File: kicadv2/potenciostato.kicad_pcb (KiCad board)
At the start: 2 copper layers, 100 x 100 mm, 56 parts, among them J1 USB_B_Micro, J10 test_GND, J11 test_GND, J12 test_GND, J13 AC2, J2 test_DAC, J3 Conn_01x03_Male, J4 test_I, J5 test_V, J6 test_VIN, J7 test_I, J8 test_V, J9 AC1, U1 OP77, U2 TL082, U3 OP77, U4 OP77, U5 4316, U6 L7805, U7 TL064, U8 L7905, U9 TL082

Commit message: movido USB
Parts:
- moved J1 23.7 mm to (199.7, 144.1)
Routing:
- net Net-(J1-Pad3): track 107.4 -> 41.7 mm, vias 1 -> 0
- net Net-(J1-Pad2): track 109.4 -> 45.7 mm, vias 1 -> 0
- net GND: track 0.00 -> 19.7 mm, vias 6 -> 16

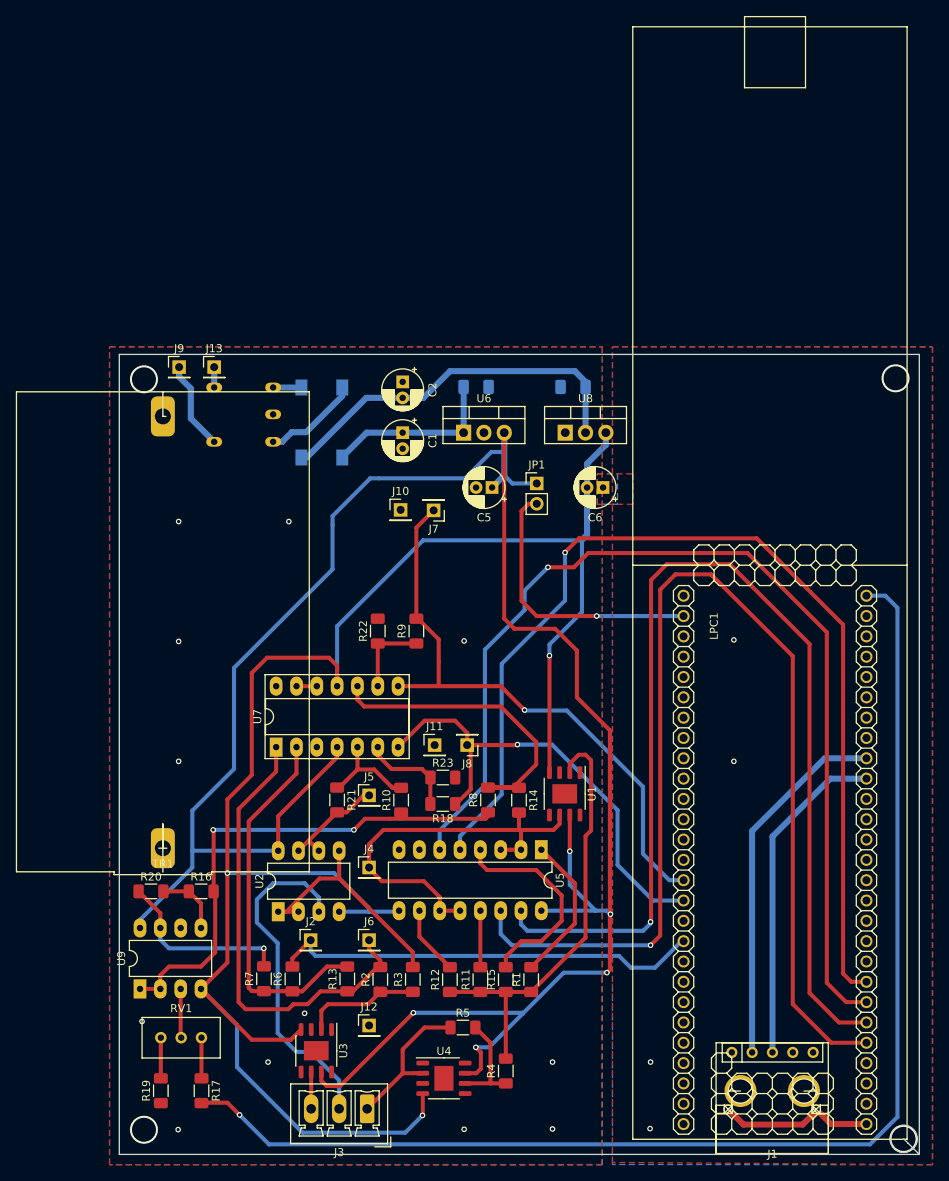
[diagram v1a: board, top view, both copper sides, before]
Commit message: agregado logo potencio al b.silk, falta generar gerber y taladro de vuelta
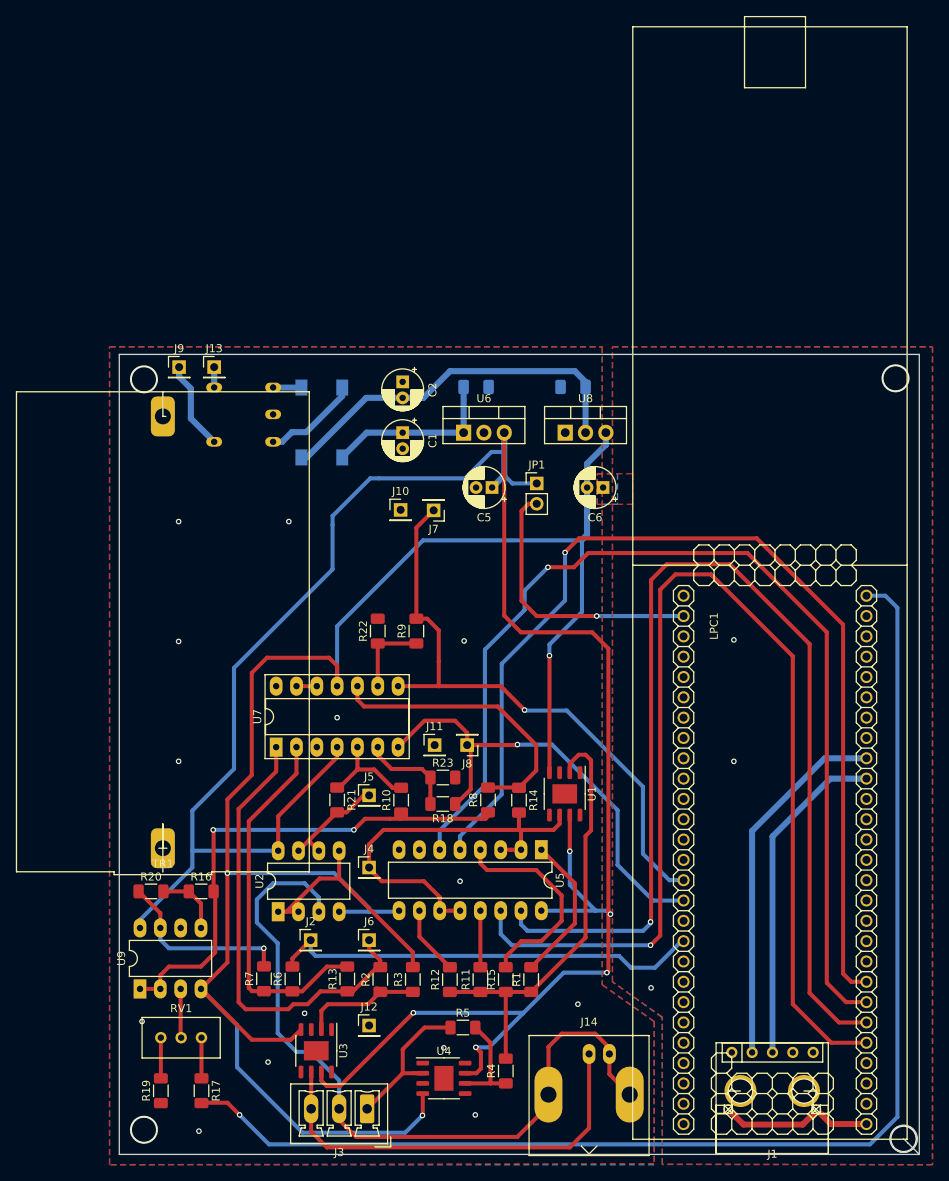
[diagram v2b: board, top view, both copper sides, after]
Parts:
- added J14: Conn_Coaxial, Connector_Coaxial:BNC_Amphenol_B6252HB-NPP3G-50_Horizontal, F.Cu at (176.8, 144.3)
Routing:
- net Net-(J14-Pad2): track 42.6 -> 95.9 mm
- net Net-(J14-Pad1): track 4.61 -> 53.3 mm
- net +5V: track 282.7 -> 285.3 mm
- net Net-(R14-Pad1): track 38.3 -> 36.5 mm
- net Net-(J7-Pad1): track 74.8 -> 75.5 mm
- net GND: vias 16 -> 17

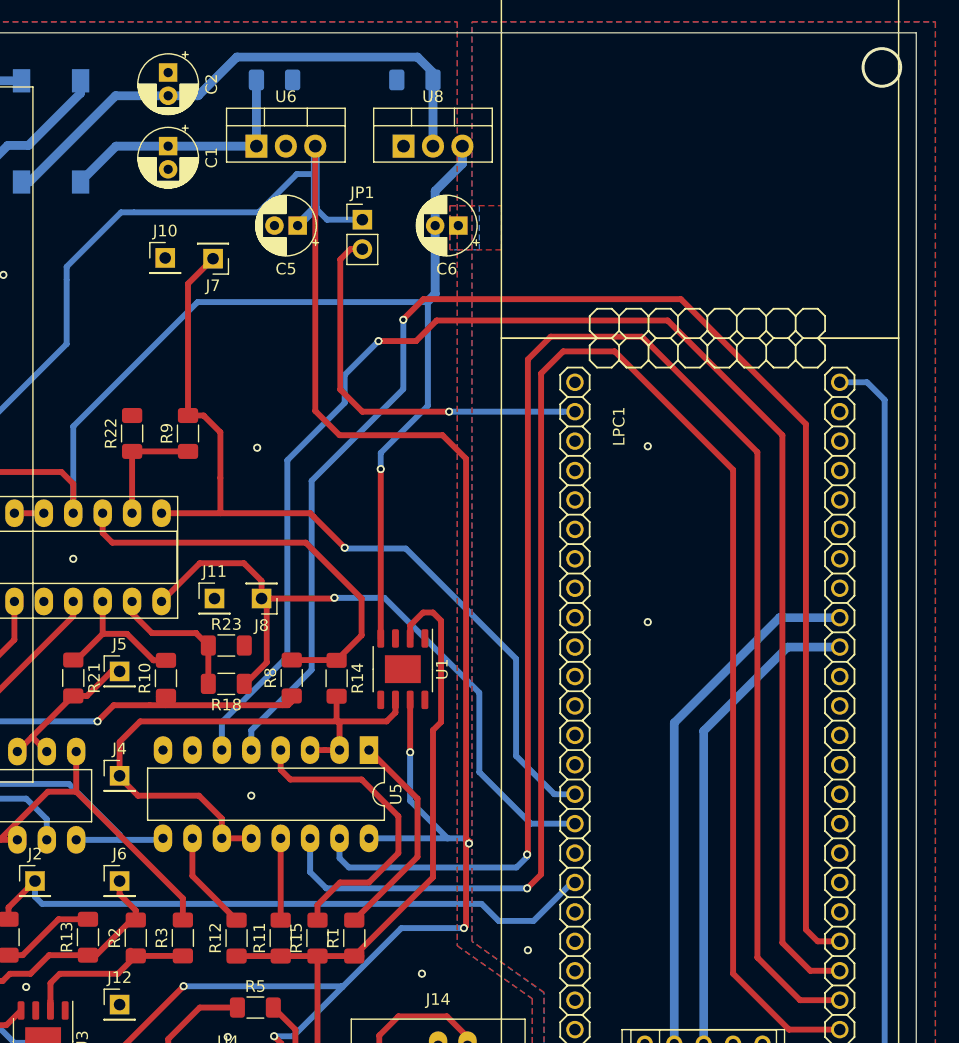
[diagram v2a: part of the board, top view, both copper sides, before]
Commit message: cambios esteticos en el silk
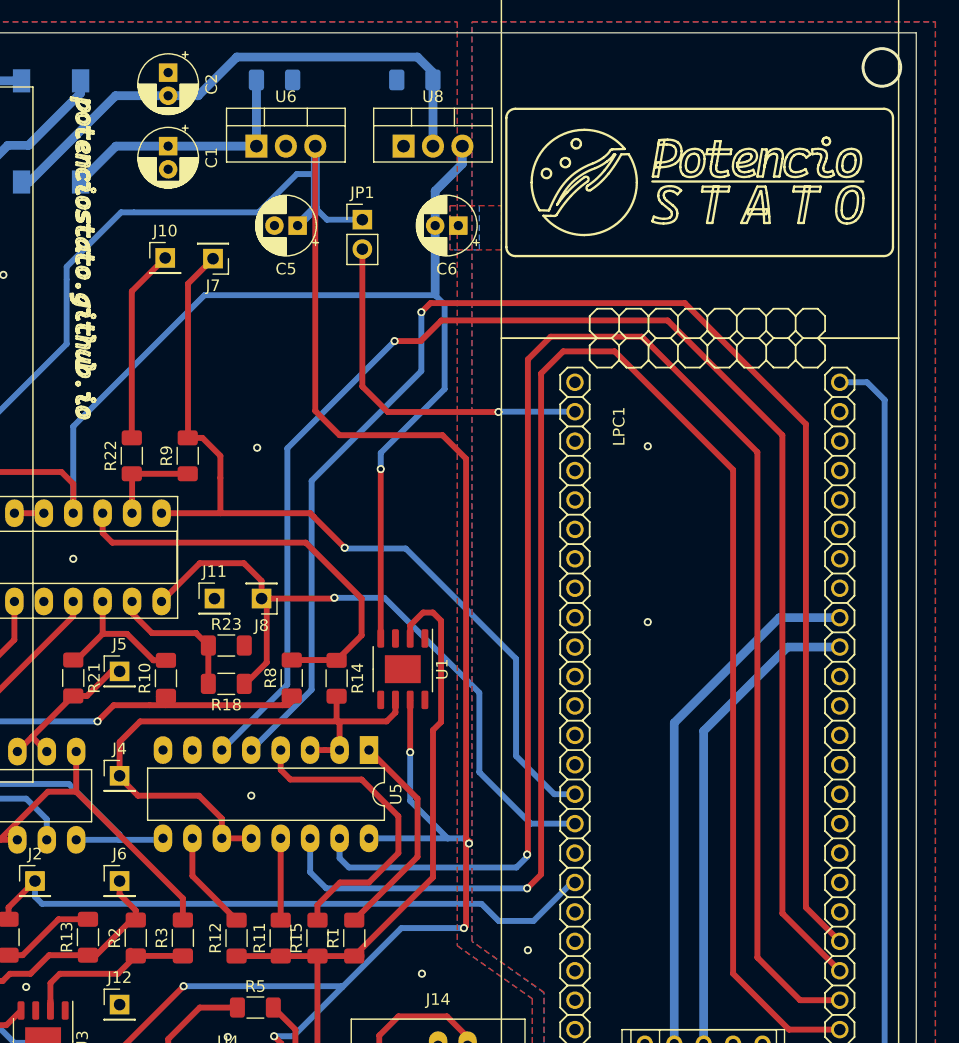
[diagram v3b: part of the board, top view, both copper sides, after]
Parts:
- moved R22 1.93 mm to (150.3, 93.3)
- moved R9 1.93 mm to (155.2, 93.3)
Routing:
- net GND: track 19.7 -> 36.4 mm
- net Net-(JP1-Pad2): track 34.6 -> 31.1 mm
- net /salida_dac/gan_x5: track 130.4 -> 128.1 mm
- net /salida_dac/gan_x1: track 129.5 -> 127.6 mm
- net Net-(R22-Pad1): track 9.98 -> 8.24 mm
- net -5V: track 229.7 -> 231.2 mm

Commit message: Se acomodó el F-silk
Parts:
- renumbered JP1 to +5V_LPC1, J9 to AC1, J13 to AC2, J3 to AUX1, J14 to BNC1, J10 to GND1, J11 to GND2, J12 to GND3, J4 to I_IN1, J2 to TP_DAC1, J7 to TP_I1, J8 to TP_V1, J1 to USB1, J6 to VIN1, J5 to V_IN1
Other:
- board text added: "REF1"
- board text added: "TRA1"

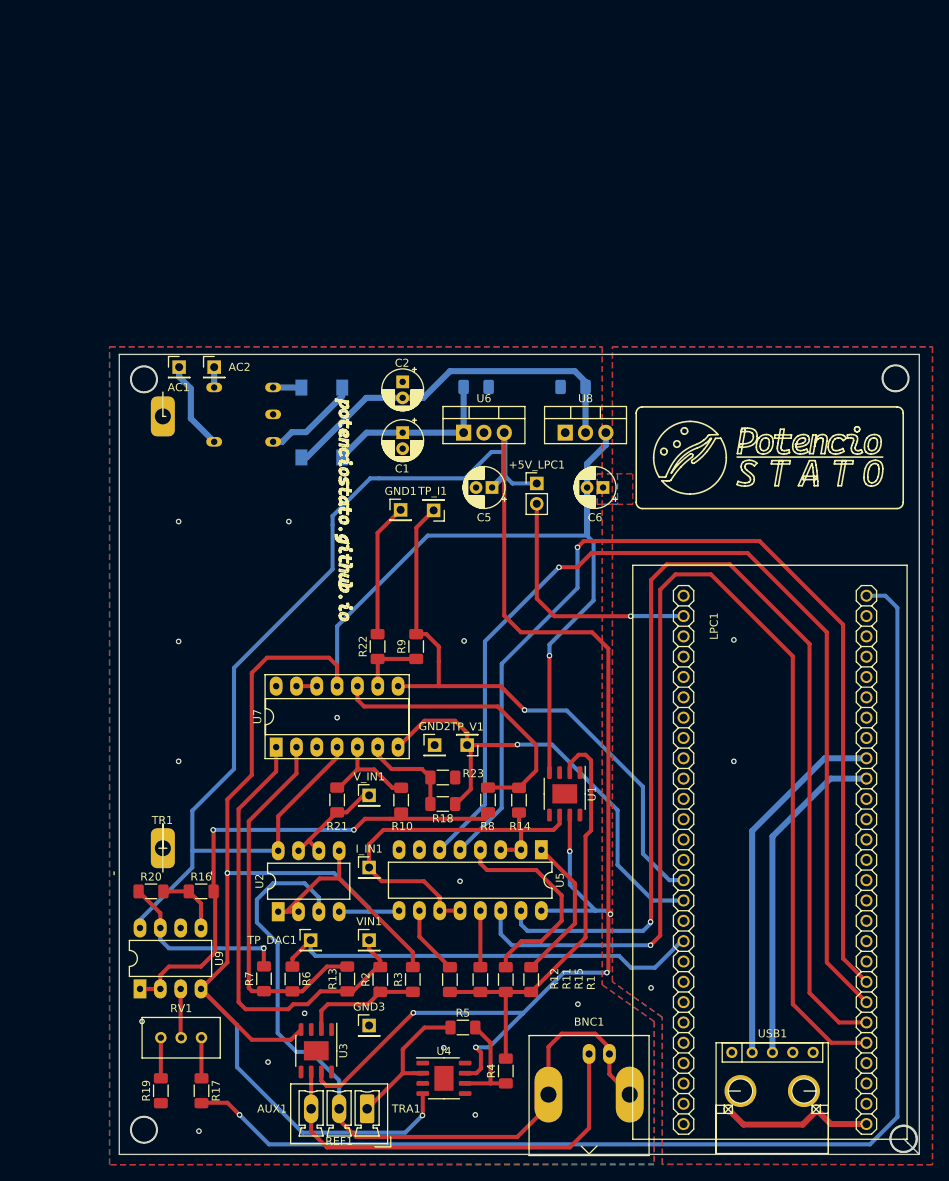
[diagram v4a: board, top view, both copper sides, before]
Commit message: cambios esteticos en fsilk
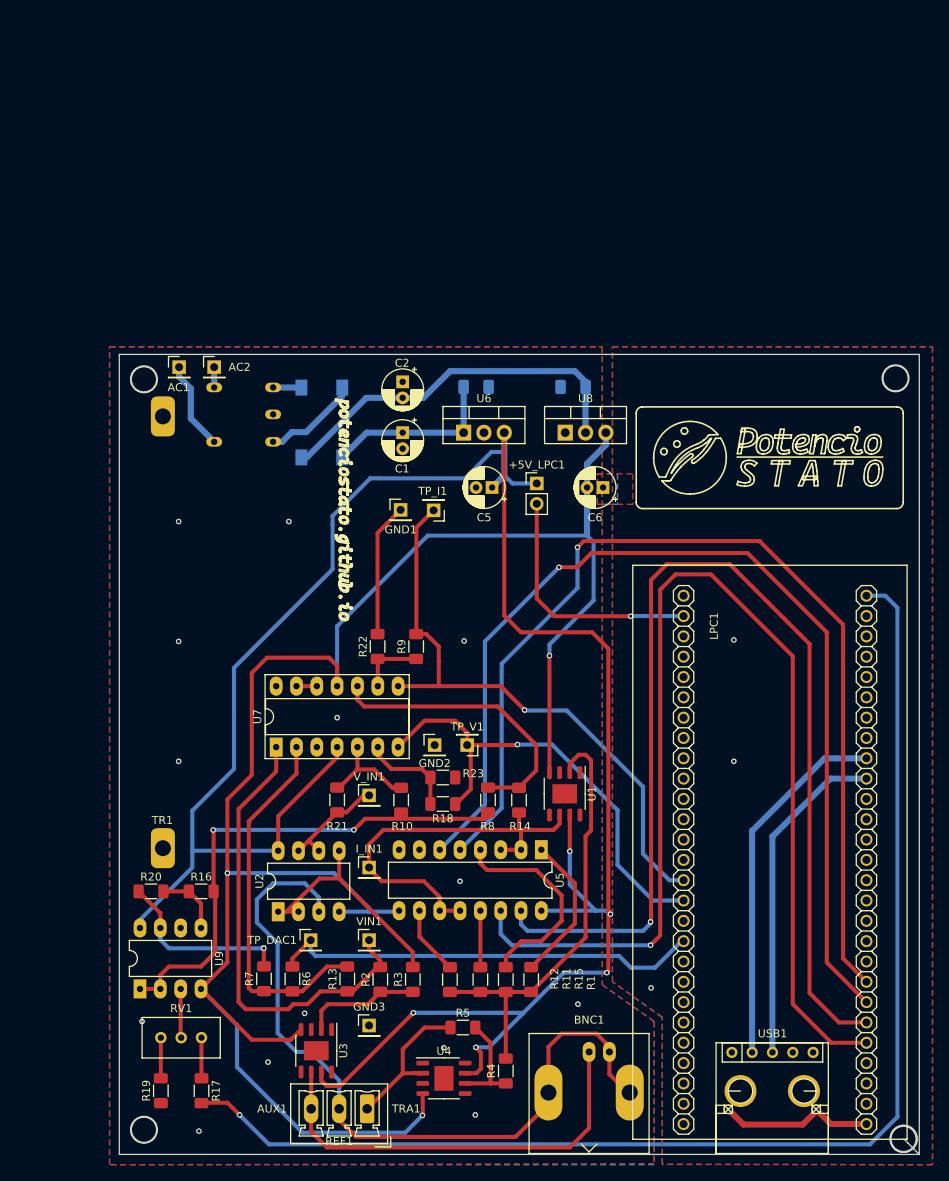
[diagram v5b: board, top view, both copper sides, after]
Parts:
- moved BNC1 0.25 mm to (176.8, 144.0)

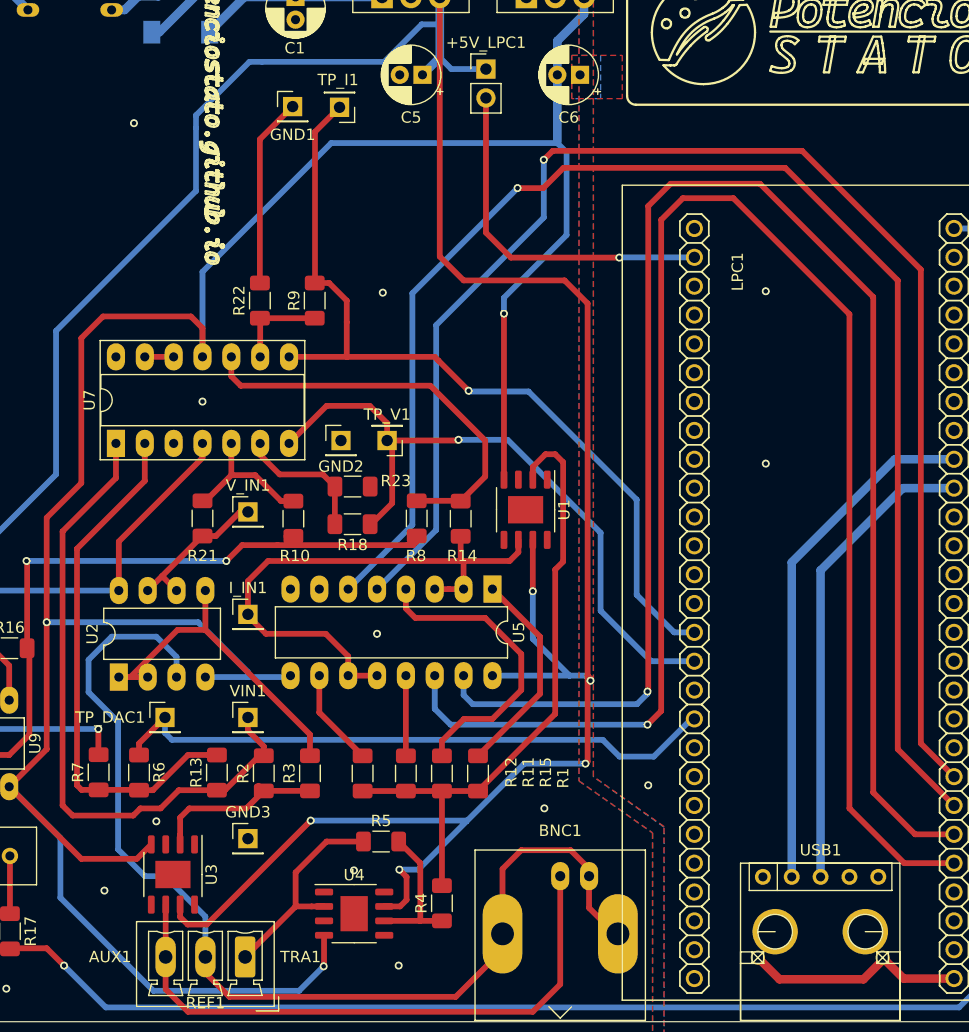
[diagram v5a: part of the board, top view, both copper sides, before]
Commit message: falta mover BNC
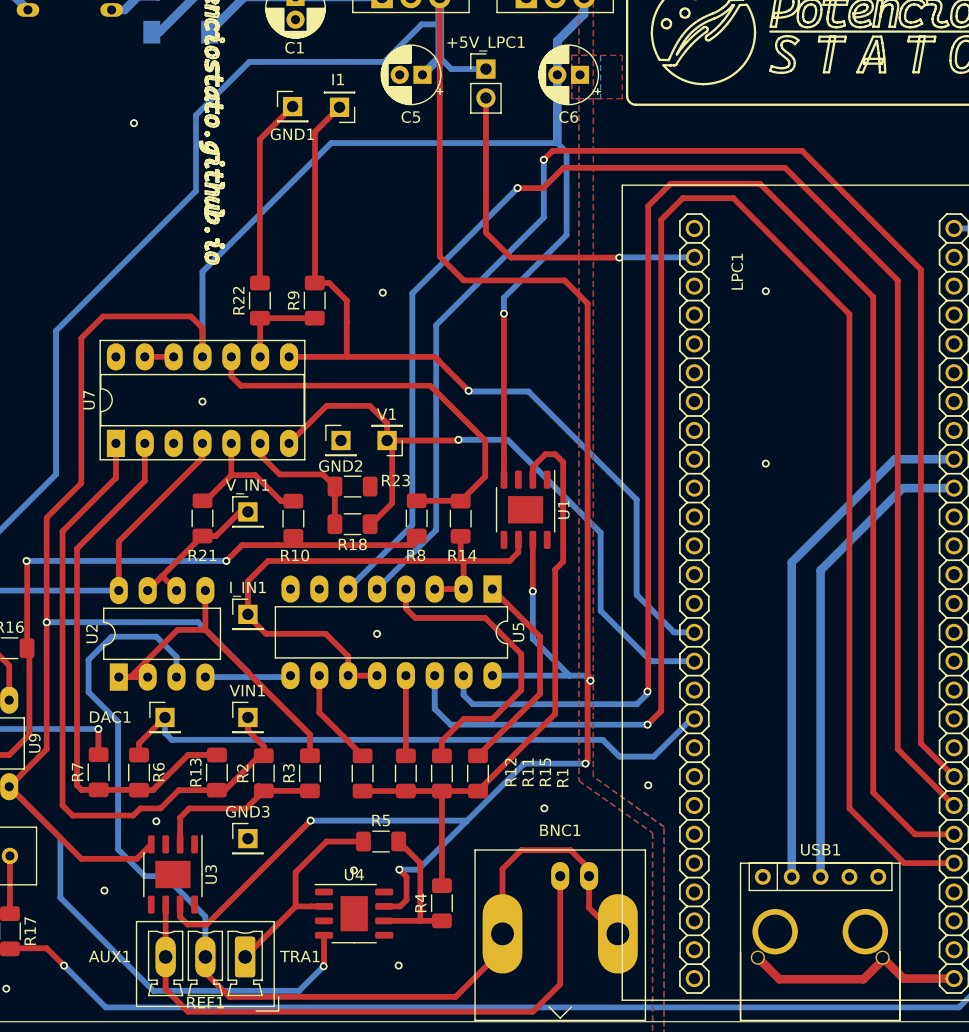
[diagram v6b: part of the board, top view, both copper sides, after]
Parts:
- renumbered TP_DAC1 to DAC1, TP_I1 to I1, TP_V1 to V1

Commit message: version final?
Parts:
- AUX1: footprint Connector_Phoenix_MC:PhoenixContact_MCV_1,5_3-G-3.5_1x03_P3.50mm_Vertical -> Connector_Phoenix_MC_HighVoltage:PhoenixContact_MCV_1,5_3-G-5.08_1x03_P5.08mm_Vertical
- moved GND2 11.6 mm to (163.1, 95.5)
- moved U7 6.04 mm to (143.5, 104.4)
- moved R9 5.09 mm to (156.2, 88.4)
- moved R22 5.04 mm to (151.1, 88.4)
- moved AC2 4.06 mm to (134.0, 58.4)
- moved AC1 4.00 mm to (129.5, 58.4)
- moved D1 3.95 mm to (147.3, 65.3)
- moved V1 3.41 mm to (163.1, 102.6)
- moved BNC1 3.17 mm to (173.6, 144.0)
- moved C1 2.54 mm to (156.0, 66.6)
- moved C2 2.54 mm to (156.0, 60.3)
- moved LPC1 1.88 mm to (194.3, 51.5)
- moved R4 1.85 mm to (164.5, 146.4)
- moved R5 1.85 mm to (159.2, 141.0)
- moved U4 1.85 mm to (156.8, 147.3)
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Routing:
- net GND: track 36.4 -> 44.7 mm, vias 17 -> 22
- net Net-(I1-Pad1): track 75.4 -> 68.3 mm
- net Net-(LPC1-Pad16): track 59.9 -> 52.9 mm
- net Net-(R13-Pad2): track 47.8 -> 53.0 mm
- net Net-(R14-Pad1): track 36.5 -> 31.7 mm
- net Net-(R22-Pad1): track 8.24 -> 12.0 mm
- net /salida_dac/VIN: track 58.0 -> 61.7 mm
- net Net-(AUX1-Pad2): track 95.9 -> 92.4 mm
- net Net-(C2-Pad2): track 46.9 -> 43.6 mm
- net Net-(R10-Pad2): track 12.7 -> 15.8 mm
- net Net-(R18-Pad2): track 12.1 -> 8.95 mm
- net Net-(+5V_LPC1-Pad2): track 31.1 -> 28.6 mm
- net Net-(C1-Pad1): track 22.2 -> 19.8 mm
- net +5V: track 285.3 -> 287.6 mm
- net Net-(AUX1-Pad1): track 18.9 -> 17.2 mm
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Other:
- outline, holes or cut-outs redrawn

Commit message: version mandada a hacer a jlcpcb
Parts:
- moved R4 5.00 mm to (164.5, 141.4)
- moved R20 3.61 mm to (122.9, 127.5)
- moved R16 3.51 mm to (128.6, 127.5)
- moved U9 3.35 mm to (122.2, 139.1)
- moved RV1 2.12 mm to (128.3, 144.4)
- moved DAC1 2.08 mm to (144.0, 130.6)
- moved R17 1.50 mm to (129.8, 149.1), turned to 0 degrees
- moved U3 1.50 mm to (142.7, 142.4), turned to 180 degrees
- moved U4 1.00 mm to (157.8, 147.3)
- moved VIN1 0.58 mm to (149.3, 130.6)
- moved R19 0.23 mm to (123.3, 149.1), turned to 0 degrees
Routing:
- net GND: track 44.7 -> 25.9 mm, vias 22 -> 21
- net Net-(AUX1-Pad2): track 92.4 -> 82.2 mm
- net /salida_dac/VOffset: track 64.2 -> 73.4 mm
- net Net-(AUX1-Pad3): track 54.4 -> 61.6 mm
- net +5V: track 287.6 -> 293.6 mm
- net Net-(R1-Pad1): track 56.7 -> 51.0 mm
- net Net-(R2-Pad1): track 15.0 -> 16.6 mm
- net Net-(R3-Pad2): track 29.2 -> 30.6 mm, vias 0 -> 1
- net Net-(DAC1-Pad1): track 55.4 -> 54.0 mm
- net Net-(R13-Pad2): track 53.0 -> 52.2 mm
- net /salida_dac/VIN: track 61.7 -> 61.0 mm
- net Net-(R16-Pad1): track 8.38 -> 7.78 mm
